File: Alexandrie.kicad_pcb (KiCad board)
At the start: 2 copper layers, 103 x 100 mm, 67 parts, among them J1 kk_10, J10 CONN_01X02, J2 kk_5, J3 kk_5, J4 CONN_01X06, J5 CONN_01X02, J6 kk_10, J7 kk_10, J8 kk_10, J9 kk_10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

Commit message: final beta, Sylkmask to annotate
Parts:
- C11, C12, C14, C15, U11: moved to B.Cu
- U12: value L4940D2T12 -> LD29150DT50R
- moved J5 61.6 mm to (77.5, 124.0), turned to 0 degrees
- moved C13 37.4 mm to (47.0, 111.5), turned to 270 degrees
- moved C15 33.7 mm to (44.5, 111.5), turned to 270 degrees
- moved C14 27.3 mm to (40.0, 112.5), turned to 270 degrees
- moved C11 23.8 mm to (22.0, 117.5), turned to 90 degrees
- moved C12 22.1 mm to (18.0, 112.5)
- moved U11 11.2 mm to (30.0, 110.0), turned to 90 degrees
- moved C19 10.3 mm to (18.0, 112.5), turned to 270 degrees
- moved U12 9.86 mm to (30.0, 110.0), turned to 90 degrees
- moved C16 8.75 mm to (44.5, 111.5)
- moved C18 8.14 mm to (22.0, 112.0), turned to 270 degrees
- moved C20 6.40 mm to (22.0, 117.5), turned to 90 degrees
- moved C17 5.70 mm to (40.0, 112.5)
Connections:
- C11 pad 2: Net-(C11-Pad2) -> +5V
- C12 pad 2: Net-(C11-Pad2) -> +5V
- C13 pad 2: Net-(C13-Pad2) -> +12V
- C14 pad 2: Net-(C13-Pad2) -> +12V
- C15 pad 2: Net-(C13-Pad2) -> +12V
- C16 pad 2: Net-(C16-Pad2) -> +12V
- C17 pad 2: Net-(C16-Pad2) -> +12V
- U11 pad 1: Net-(C13-Pad2) -> +12V
- U11 pad 3: Net-(C11-Pad2) -> +5V
- U12 pad 3: Net-(C16-Pad2) -> +12V
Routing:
- net GND: track 139.3 -> 491.1 mm, vias 49 -> 172
- net +12V: track 249.5 -> 349.9 mm, vias 4 -> 5
- net +5V: track 417.4 -> 481.3 mm
- net Net-(C18-Pad2): track 22.0 -> 83.8 mm
- net Net-(C16-Pad2): track 27.2 -> 0.00 mm
- net Net-(C11-Pad2): track 25.1 -> 0.00 mm
- net Net-(C13-Pad2): track 13.0 -> 0.00 mm

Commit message: RTM with sylkmask
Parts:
- removed TP1, TP2: TEST, Mounting_Holes:MountingHole_3.5mm_Pad
- added ?: , Mounting_Holes:MountingHole_3.5mm_Pad, F.Cu at (112.0, 33.0)
- added ?: , Mounting_Holes:MountingHole_3.5mm_Pad, F.Cu at (19.0, 123.0)
- added ?: , Mounting_Holes:MountingHole_3.5mm_Pad, F.Cu at (19.0, 33.0)
- added ?: , Mounting_Holes:MountingHole_3.5mm_Pad, F.Cu at (112.0, 123.0)
- added D9: D, Diodes_SMD:D_SMB_Handsoldering, B.Cu at (63.0, 122.0)
- added J11: , conn_kk100:kk100_22-23-2031, F.Cu at (70.0, 124.0)
- added REF***: OSHW-Logo_11.4x12mm_SilkScreen, Symbols:OSHW-Logo_11.4x12mm_SilkScreen, F.Cu at (98.0, 40.0)
- C13, C16: moved to B.Cu
- J1, J6, J7, J8, J9: value kk_10 -> (none)
- J10, J5: value CONN_01X02 -> (none)
- J2, J3: value kk_5 -> (none)
- J4: value CONN_01X06 -> (none)
- moved C20 33.1 mm to (55.0, 115.0), turned to 270 degrees
- moved C18 31.1 mm to (53.0, 115.0)
- moved C19 31.0 mm to (49.0, 112.0)
- moved C16 15.6 mm to (55.0, 123.0), turned to 90 degrees
- moved D2 13.2 mm to (48.0, 100.0)
- moved C13 13.0 mm to (53.0, 123.0), turned to 90 degrees
- moved C12 12.0 mm to (30.0, 113.0)
- moved J6 11.0 mm to (112.0, 53.0)
- moved U11 10.8 mm to (39.0, 116.0)
- moved U12 10.8 mm to (39.0, 116.0)
- moved C17 10.0 mm to (30.0, 113.0)
- moved J7 10.0 mm to (112.0, 79.0)
- moved C15 9.19 mm to (53.0, 115.0)
- moved C14 9.01 mm to (49.0, 112.0)
- moved C11 8.50 mm to (26.0, 110.0), turned to 270 degrees
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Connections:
- U12 pad 1: Net-(C18-Pad2) -> +12V
- U12 pad 3: +12V -> Net-(C18-Pad2)
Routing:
- net GND: track 491.1 -> 556.7 mm, vias 172 -> 166
- net Net-(C18-Pad2): track 83.8 -> 49.6 mm
- net +5V: track 481.3 -> 448.0 mm, vias 22 -> 18
- net +12V: track 349.9 -> 365.6 mm, vias 5 -> 7
- net Net-(D2-Pad1): track 17.4 -> 3.09 mm, vias 2 -> 0
- net 20HPF: track 78.1 -> 92.4 mm
- net 30/20m_2: track 51.9 -> 65.8 mm
- net 13HPF: track 77.9 -> 90.7 mm
- net 40m_2: track 56.2 -> 68.7 mm
- net 17/15m_2: track 36.3 -> 47.3 mm
- net 12/10m_2: track 32.6 -> 43.4 mm
- net 6mLNA: track 70.3 -> 80.9 mm, vias 2 -> 3
- net 6m_2: track 29.4 -> 39.9 mm
- net 9.5HPF: track 66.1 -> 76.4 mm
- net 80m_2: track 62.0 -> 71.3 mm
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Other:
- board text added: "+12V Gnd Ant_1 Ant_2 Ant_3"
- board text added: "- + 12V In +"
- board text added: "- + 5V Out"
- board text added: "1"
- board text added: "10"
- board text added: "12V In"
- board text added: "160m 80m 40m 30/20m 17/15m 12/10m 6m Gnd +12V Gnd"
- board text added: "20_HPF 13_HPF 9.5_HPF 6.5_HPF 1.5_HPF 6m_LSA RX2_Gnd HPF_Bypass +12V Gnd"
- board text added: "5"
- board text added: "5V Out"
- board text added: "6"
- board text added: "Alexandrie dual hpf/lpf filter Control Board for Angelia"
- board text added: "Alternate TX/RX Relay cmd"
- board text added: "Ant_Tune +1V Alex SPI_SDO SPI_SCK SPI_RX_Load SPI_TX_Load FWD_PWR PTT REFL_PWR Gnd"
- board text added: "Antenna Cont."
- board text added: "FWD_PWR REFL_PWR Gnd +12V TX_RX_RLY TXRX_Status"
- board text added: "From Alex Conn. on Angelia Brd"
- board text added: "From VSWR/TX-RX PureSig. cplr"
- board text added: "Original design by Graham Haddock, KE9H and Phil Harman, VK6APH Drawing & mods by f6itu"
- board text added: "To HPF1 Board"
- board text added: "To HPF2 Board"
- board text added: "To LPF_1 board"
- board text added: "To LPF_2 board"
- board text added: "To Mentor Arduino Ctrl Brd"
- board text added: "https://github.com/F6ITU https://wiki.electrolab.fr/Projets:Lab:2017:Peripheriques_Angelia"

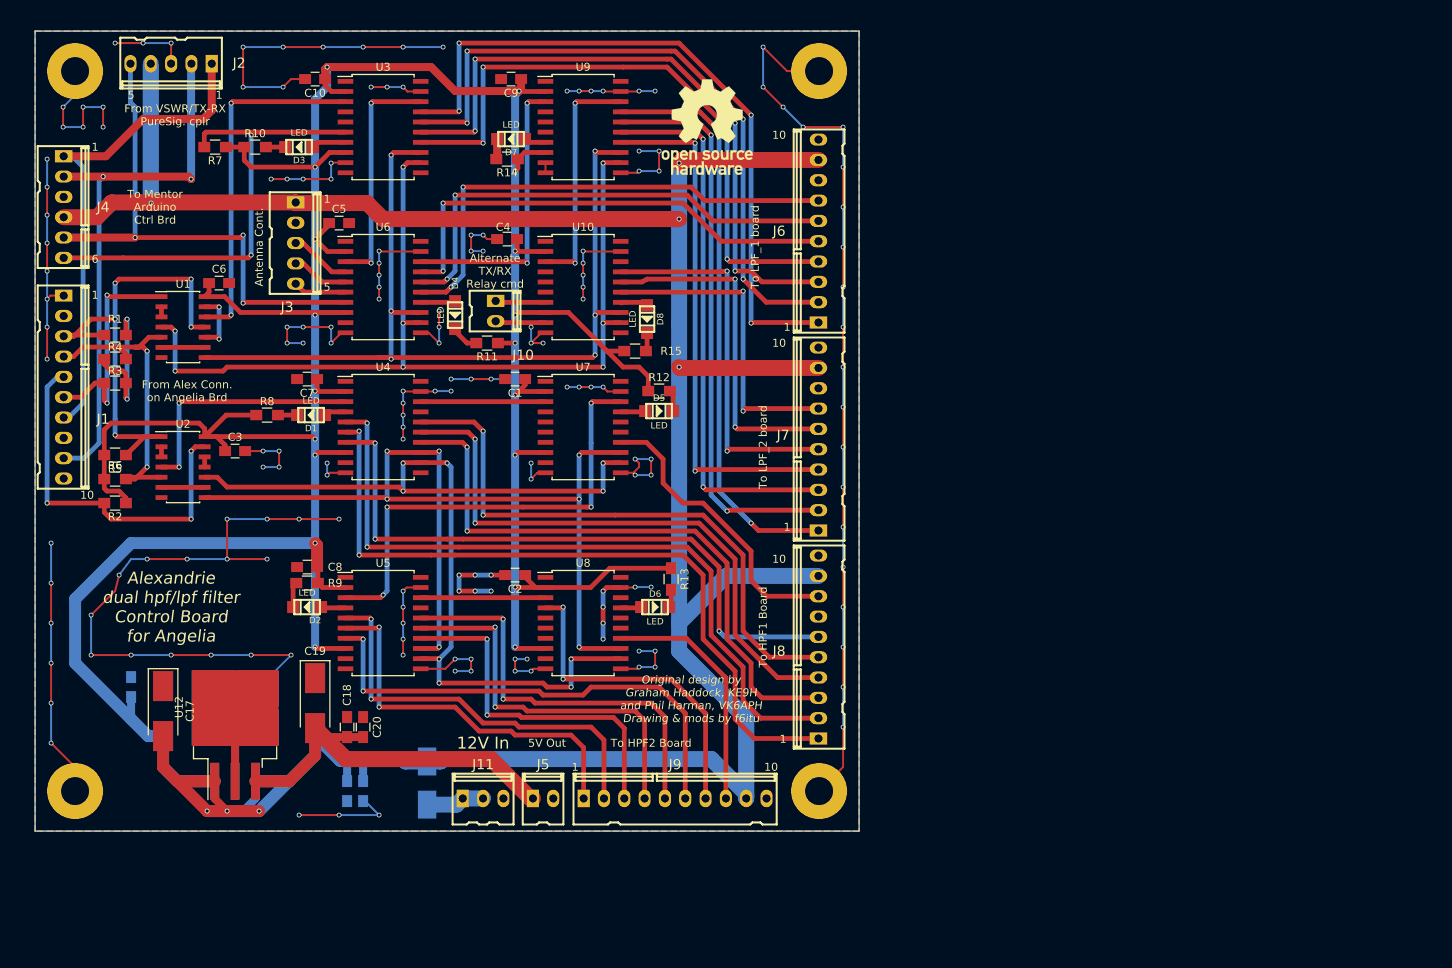
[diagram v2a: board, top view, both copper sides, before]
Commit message: Complete redrawing, Alexiares compatible
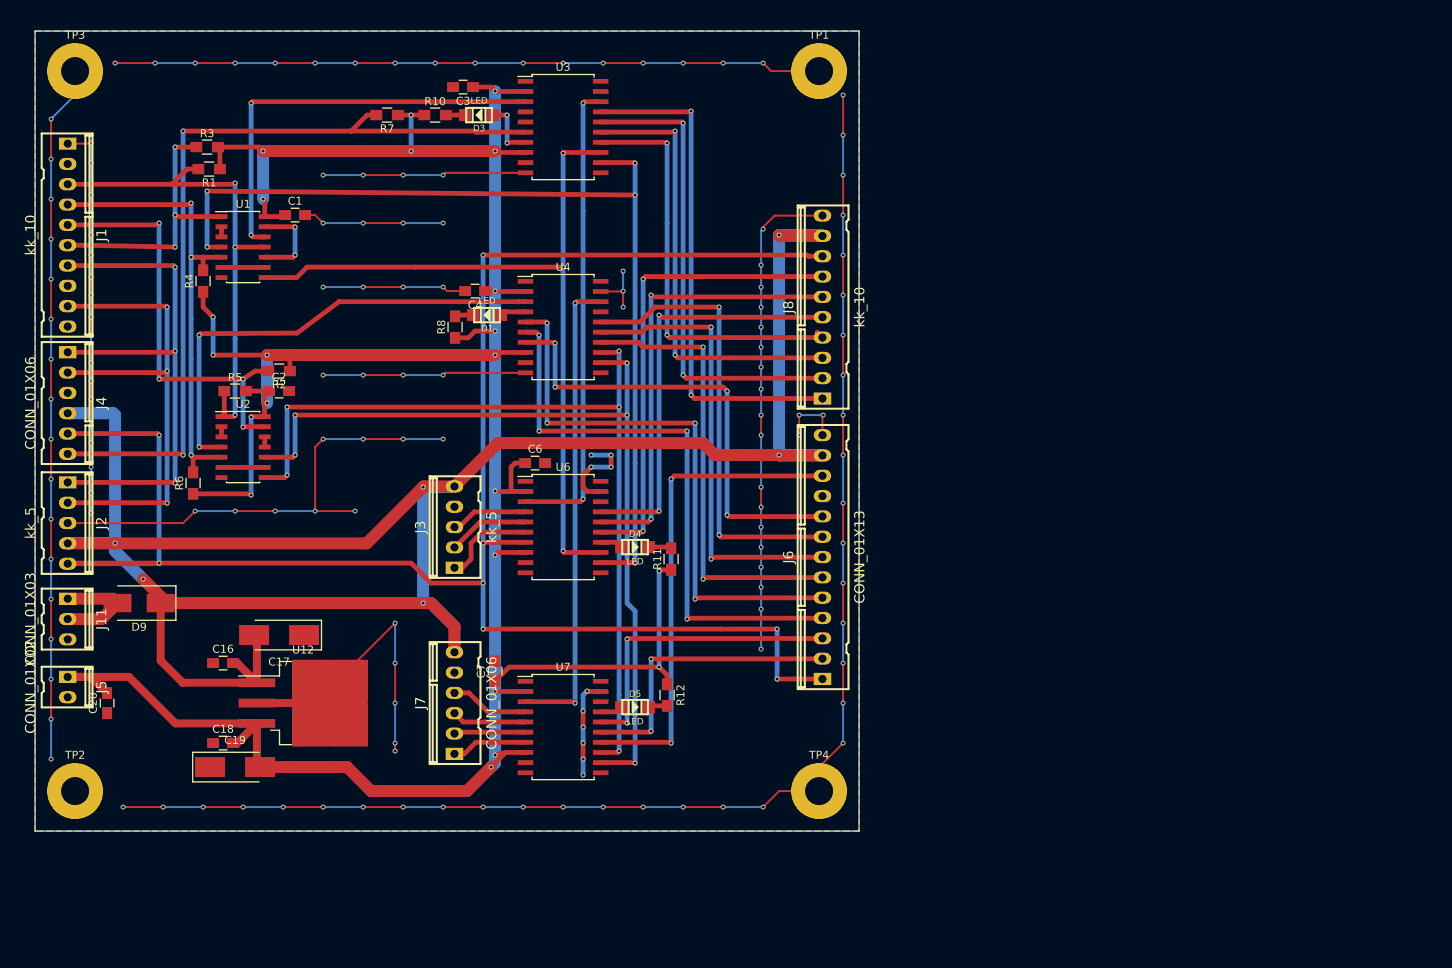
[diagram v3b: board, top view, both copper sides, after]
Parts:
- removed ? (x4): , Mounting_Holes:MountingHole_3.5mm_Pad
- removed C10, C11, C13, C15, C5, C8, C9: 100n, Capacitors_SMD:C_0805_HandSoldering
- removed C12, C14: 10u, Capacitors_Tantalum_SMD:CP_Tantalum_Case-C_EIA-6032-28_Hand
- removed D2, D6, D7, D8: LED, smd_leds:Led_1206
- removed J10: , conn_kk100:kk100_22-23-2021
- removed J9: , conn_kk100:kk100_22-23-2101
- removed R13, R14, R15, R9: 1k2, Resistors_SMD:R_0805_HandSoldering
- removed REF***: OSHW-Logo_11.4x12mm_SilkScreen, Symbols:OSHW-Logo_11.4x12mm_SilkScreen
- removed U10, U5, U8, U9: TPIC6B595, Housings_SOIC:SOIC-20W_7.5x12.8mm_Pitch1.27mm
- removed U11: LD29150DT50R, TO_SOT_Packages_SMD:TO-263-3_TabPin4
- added TP1: TEST, Mounting_Holes:MountingHole_3.5mm_Pad, F.Cu at (112.0, 33.0)
- added TP2: TEST, Mounting_Holes:MountingHole_3.5mm_Pad, F.Cu at (19.0, 123.0)
- added TP3: TEST, Mounting_Holes:MountingHole_3.5mm_Pad, F.Cu at (19.0, 33.0)
- added TP4: TEST, Mounting_Holes:MountingHole_3.5mm_Pad, F.Cu at (112.0, 123.0)
- C16, D9: moved to F.Cu
- J1, J8: value (none) -> kk_10
- J11: value (none) -> CONN_01X03
- J2, J3: value (none) -> kk_5
- J4: value (none) -> CONN_01X06
- J5: value (none) -> CONN_01X02
- J6: value (none) -> CONN_01X13; footprint conn_kk100:kk100_22-23-2101 -> conn_kk100:kk100_22-23-2131
- J7: value (none) -> CONN_01X06; footprint conn_kk100:kk100_22-23-2101 -> conn_kk100:kk100_22-23-2061
- moved J5 61.1 mm to (18.0, 110.0), turned to 270 degrees
- moved J2 59.0 mm to (18.0, 89.5), turned to 270 degrees
- moved J11 56.7 mm to (18.0, 101.5), turned to 270 degrees
- moved J7 56.2 mm to (66.5, 112.0)
- moved C3 53.7 mm to (67.5, 35.0), turned to 180 degrees
- moved C6 45.5 mm to (76.5, 82.0)
- moved C7 43.4 mm to (71.5, 108.0), turned to 90 degrees
- moved J8 42.5 mm to (112.5, 62.5)
- moved D9 42.5 mm to (27.0, 99.5), turned to 180 degrees
- moved J6 40.8 mm to (112.5, 93.8)
- moved J3 40.7 mm to (66.5, 90.0), turned to 90 degrees
- moved R12 38.0 mm to (93.0, 111.0), turned to 270 degrees
- moved U7 37.6 mm to (80.0, 115.0)
- moved U6 37.5 mm to (80.0, 90.0)
- moved C2 37.4 mm to (44.5, 73.0), turned to 0 degrees
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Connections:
- net Net-(J3-Pad3) renamed Ant_1
- C18 pad 2: Net-(C18-Pad2) -> +5V
- C19 pad 2: Net-(C18-Pad2) -> +5V
- C20 pad 2: Net-(C18-Pad2) -> +5V
- J3 pad 1: +12V -> Ant_3
- J3 pad 2: GND -> Ant_2
- J3 pad 4: Net-(J3-Pad4) -> GND
- J3 pad 5: Net-(J3-Pad5) -> +12V
- J5 pad 1: Net-(C18-Pad2) -> +5V
- J6 pad 1: 160m -> TX_RX_RLY
- J6 pad 2: 80m -> Att1
- J6 pad 3: 40m -> Att2
- J6 pad 4: 30/20m -> 20HPF
- J6 pad 5: 17/15m -> 13HPF
- J6 pad 6: 12/10m -> 9.5HPF
- J6 pad 7: 6m -> 6.5HPF
- J6 pad 8: GND -> 1.5HPF
- J6 pad 9: +12V -> 6mLNA
- J7 pad 1: 160m_2 -> RX_BYPASS_OUT
- J7 pad 2: 80m_2 -> RX3_IN
- J7 pad 3: 40m_2 -> RX2_IN
- J7 pad 4: 30/20m_2 -> Xvtr_IN
- J7 pad 5: 17/15m_2 -> GND
- J7 pad 6: 12/10m_2 -> +12V
- J8 pad 1: 20HPF -> 160m
- J8 pad 2: 13HPF -> 80m
- J8 pad 3: 9.5HPF -> 40m
- J8 pad 4: 6.5HPF -> 30/20m
- J8 pad 5: 1.5HPF -> 17/15m
- J8 pad 6: 6mLNA -> 12/10m
- J8 pad 7: (no net) -> 6m_Bypass
- J8 pad 8: HPF_ByPass -> TX_RX_RLY
- R1 pad 1: Net-(R1-Pad1) -> +5V
- R3 pad 2: Net-(R1-Pad1) -> +5V
- R4 pad 1: Net-(R1-Pad1) -> +5V
- U12 pad 3: Net-(C18-Pad2) -> +5V
- U6 pad 15: 6m -> 6m_Bypass
- U6 pad 18: Net-(U6-Pad18) -> (no net)
- U6 pad 5: Net-(J3-Pad4) -> Ant_2
- U6 pad 6: Net-(J3-Pad5) -> Ant_3
- U7 pad 15: (no net) -> Att1
- U7 pad 16: (no net) -> Att2
- U7 pad 18: Net-(U5-Pad3) -> (no net)
- U7 pad 4: (no net) -> Xvtr_IN
- U7 pad 5: (no net) -> RX2_IN
- U7 pad 6: (no net) -> RX3_IN
- U7 pad 7: (no net) -> RX_BYPASS_OUT
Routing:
- net TX_RX_RLY: track 65.9 -> 235.2 mm, vias 3 -> 8
- net GND: track 556.7 -> 687.6 mm, vias 166 -> 150
- net +12V: track 365.6 -> 281.0 mm, vias 7 -> 6
- net 160m_2: track 72.8 -> 0.00 mm, vias 2 -> 0
- net 80m_2: track 71.3 -> 0.00 mm, vias 2 -> 0
- net 40m_2: track 68.7 -> 0.00 mm, vias 2 -> 0
- net +5V: track 448.0 -> 381.4 mm, vias 18 -> 22
- net 30/20m_2: track 65.8 -> 0.00 mm, vias 2 -> 0
- net 6m: track 62.3 -> 0.00 mm, vias 2 -> 0
- net 6mLNA_2: track 61.6 -> 0.00 mm, vias 2 -> 0
- net 6m_Bypass: track 0.00 -> 59.4 mm, vias 0 -> 2
- net Net-(U5-Pad3): track 58.3 -> 0.00 mm, vias 4 -> 0
- net 13HPF_2: track 52.0 -> 0.00 mm, vias 2 -> 0
- net 1.5HPF_2: track 51.7 -> 0.00 mm, vias 2 -> 0
- net Net-(C18-Pad2): track 49.6 -> 0.00 mm
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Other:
- board text removed: "+12V Gnd Ant_1 Ant_2 Ant_3"
- board text removed: "- + 12V In +"
- board text removed: "- + 5V Out"
- board text removed: "1"
- board text removed: "10"
- board text removed: "12V In"
- board text removed: "160m 80m 40m 30/20m 17/15m 12/10m 6m Gnd +12V Gnd"
- board text removed: "20_HPF 13_HPF 9.5_HPF 6.5_HPF 1.5_HPF 6m_LSA RX2_Gnd HPF_Bypass +12V Gnd"
- board text removed: "5"
- board text removed: "5V Out"
- board text removed: "6"
- board text removed: "Alexandrie dual hpf/lpf filter Control Board for Angelia"
- board text removed: "Alternate TX/RX Relay cmd"
- board text removed: "Ant_Tune +1V Alex SPI_SDO SPI_SCK SPI_RX_Load SPI_TX_Load FWD_PWR PTT REFL_PWR Gnd"
- board text removed: "Antenna Cont."
- board text removed: "FWD_PWR REFL_PWR Gnd +12V TX_RX_RLY TXRX_Status"
- board text removed: "From Alex Conn. on Angelia Brd"
- board text removed: "From VSWR/TX-RX PureSig. cplr"
- board text removed: "Original design by Graham Haddock, KE9H and Phil Harman, VK6APH Drawing & mods by f6itu"
- board text removed: "To HPF1 Board"
- board text removed: "To HPF2 Board"
- board text removed: "To LPF_1 board"
- board text removed: "To LPF_2 board"
- board text removed: "To Mentor Arduino Ctrl Brd"
- board text removed: "https://github.com/F6ITU https://wiki.electrolab.fr/Projets:Lab:2017:Peripheriques_Angelia"

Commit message: some minor cleaning
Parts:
-  : renamed from TP1; value TEST -> (none)
-  : renamed from TP2; value TEST -> (none)
-  : renamed from TP3; value TEST -> (none)
-  : renamed from TP4; value TEST -> (none)
- J1, J8: value kk_10 -> (none)
- J11: value CONN_01X03 -> (none)
- J2, J3: value kk_5 -> (none)
- J4, J7: value CONN_01X06 -> (none)
- J5: value CONN_01X02 -> (none)
- J6: value CONN_01X13 -> (none)
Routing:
- net GND: track 687.6 -> 726.7 mm, vias 150 -> 154
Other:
- board text added: "+12V Gnd Ant_1 Ant_2 Ant_3"
- board text added: "+12V Gnd Xvtr_IN RX2_IN RX3_IN RX_ByPass_OUT"
- board text added: "+12V In +12V In Gnd"
- board text added: "+5V Out Gnd"
- board text added: "160m 80m 40m 30/20m 17/15m 12/10m 6m Gnd +12V Gnd"
- board text added: "Ant_Tune +12V Alex SPI_SDO SPI_SCK SPI_RX_Load SPI_TX_Load FWD_PWR PTT REFL_PWR GND"
- board text added: "FWD_PWR REFL_PWR Gnd +12V TX_RX_RLY"
- board text added: "FWD_PWR REFL_PWR Gnd +12V TX_RX_RLY TXRX_Status"
- board text added: "TX_RX_RLY Att1 Att2 20HPF 13HPF 9.5HPF 6.5HPF 1.5HPF 6mLNA Gnd HPF_ByPass +12V Gnd"

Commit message: RTM 1
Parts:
- moved   76.5 mm to (94.0, 138.0)
- moved   76.5 mm to (94.0, 48.0)
- moved C1 75.5 mm to (120.5, 66.0)
- moved C16 75.5 mm to (111.5, 122.0)
- moved C17 75.5 mm to (118.5, 118.5)
- moved C18 75.5 mm to (111.5, 132.0)
- moved C19 75.5 mm to (113.0, 135.0)
- moved C2 75.5 mm to (118.5, 88.0)
- moved C20 75.5 mm to (97.0, 127.0)
- moved C3 75.5 mm to (141.5, 50.0)
- moved C4 75.5 mm to (143.0, 75.5)
- moved C6 75.5 mm to (150.5, 97.0)
- moved C7 75.5 mm to (145.5, 123.0)
- moved D1 75.5 mm to (144.5, 78.5)
- moved D3 75.5 mm to (143.5, 53.5)
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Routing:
- net +12V: track 281.0 -> 271.3 mm
- net GND: track 726.7 -> 718.0 mm, vias 154 -> 151
- net TX_RX_RLY: track 235.2 -> 232.5 mm
- net 30/20m: track 52.8 -> 50.4 mm
- net 40m: track 55.9 -> 54.4 mm
- net 17/15m: track 52.4 -> 50.9 mm
- net 6m_Bypass: track 59.4 -> 57.9 mm
- net 160m: track 63.4 -> 61.9 mm
- net 12/10m: track 56.0 -> 54.5 mm
- net 80m: track 59.4 -> 57.9 mm
- net 6mLNA: track 58.4 -> 57.0 mm
- net 1.5HPF: track 57.1 -> 55.7 mm
- net 20HPF: track 72.8 -> 71.4 mm
- net 13HPF: track 71.7 -> 70.3 mm
- net Att1: track 36.8 -> 35.4 mm
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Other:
- board size 103 x 100 mm -> 100 x 100 mm
